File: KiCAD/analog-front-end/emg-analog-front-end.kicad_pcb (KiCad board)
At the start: 2 copper layers, 45 x 20 mm, 42 parts, among them J1 Conn_01x03, J2 Conn_01x03, J4 Conn_01x03_Female, J5 Conn_01x03_Female, J6 Conn_01x03_Female, J7 Conn_01x03_Female, U1 AD620, U2 LMC6482, U3 LMC6482, U4 LMC6482

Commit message: more progress on layout
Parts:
- added J3: Conn_01x03, Connector_PinHeader_1.27mm:PinHeader_1x03_P1.27mm_Vertical, F.Cu at (28.0, 18.5)
- moved C13 23.6 mm to (25.5, 15.9), turned to 90 degrees
- moved C16 19.7 mm to (35.8, 5.59), turned to 90 degrees
- moved J2 17.5 mm to (28.0, 1.50), turned to 90 degrees
- moved C12 14.5 mm to (35.1, 11.6), turned to 180 degrees
- moved C17 13.8 mm to (26.7, 9.40), turned to 90 degrees
- moved TP1 8.13 mm to (16.1, 3.17)
- moved R11 7.66 mm to (33.1, 2.29)
- moved R10 6.65 mm to (33.1, 1.14), turned to 0 degrees
- moved C8 6.52 mm to (10.5, 11.7), turned to -90 degrees
- moved R8 5.90 mm to (34.8, 1.65), turned to -90 degrees
- moved C7 5.35 mm to (11.7, 11.7), turned to -90 degrees
- moved C6 4.47 mm to (12.8, 11.7), turned to -90 degrees
- moved C5 4.07 mm to (14.0, 11.7), turned to -90 degrees
- moved H2 3.05 mm to (39.0, 17.0)
- moved H3 3.04 mm to (39.0, 3.00)
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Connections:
- net /AOUT_CH0 renamed AOUT_CH0
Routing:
- net AOUT_CH0: track 0.00 -> 24.2 mm
- net /AMP_IN-_CH0: track 0.00 -> 17.7 mm, vias 0 -> 2
- net VDD: track 0.00 -> 17.5 mm, vias 0 -> 2
- net /AMP_OUT_CH0: track 0.00 -> 17.0 mm, vias 0 -> 2
- net SK11: track 0.00 -> 11.6 mm
- net -5V: track 0.00 -> 7.82 mm
- net Net-(C10-Pad2): track 0.00 -> 7.79 mm, vias 0 -> 2
- net /AMP_IN+_CH0: track 0.00 -> 7.27 mm
- net SK01: track 0.00 -> 6.88 mm
- net Net-(C11-Pad1): track 0.00 -> 4.17 mm
- net /NOTCH_IN_CH0: track 0.00 -> 4.15 mm
- net SK00: track 0.00 -> 4.15 mm
- net /IA_OUT_CH0: track 0.00 -> 3.43 mm
- net /HPF_OUT_CH0: track 0.00 -> 3.43 mm
- net NOTCH_OUT_CH0: track 0.00 -> 3.42 mm
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- added copper zone on F.Cu, net GND
- added copper zone on B.Cu, net VDD
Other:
- board size 45 x 20 mm -> 42 x 20 mm
- board text added: "E+"
- board text added: "E-"
- board text added: "REF"

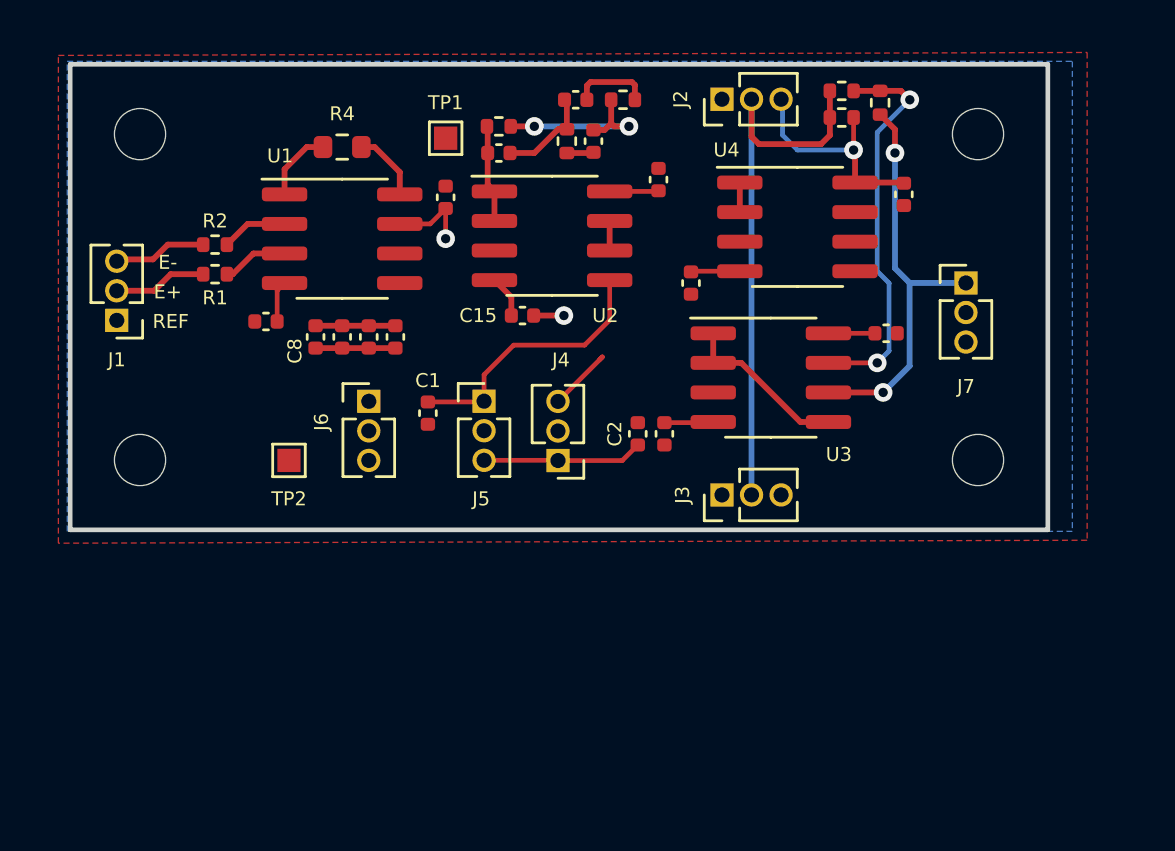
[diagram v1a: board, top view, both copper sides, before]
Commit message: AFE sub-circuit layout done
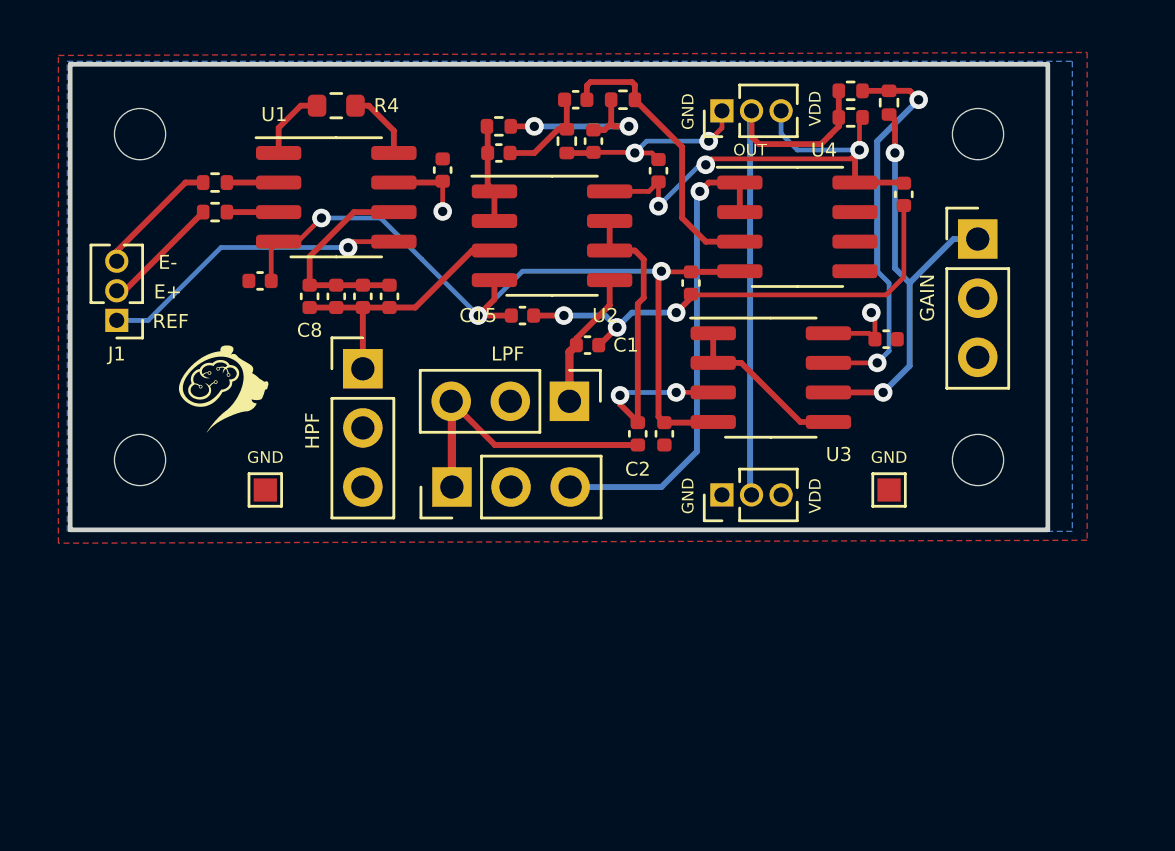
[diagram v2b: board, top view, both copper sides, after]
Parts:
- added G***: LOGO, LOGO, F.Cu at (6.60, 14.0)
- J4, J5, J6, J7: footprint Connector_PinHeader_1.27mm:PinHeader_1x03_P1.27mm_Vertical -> Connector_PinHeader_2.54mm:PinHeader_1x03_P2.54mm_Vertical
- moved TP1 24.3 mm to (35.2, 18.3)
- moved C1 7.45 mm to (22.2, 12.1), turned to 180 degrees
- moved J4 4.70 mm to (16.4, 18.2), turned to 90 degrees
- moved J5 3.67 mm to (21.4, 14.5), turned to -90 degrees
- moved R1 2.67 mm to (6.22, 6.35)
- moved R2 2.67 mm to (6.22, 5.08)
- moved J7 1.95 mm to (39.0, 7.51)
- moved U1 1.80 mm to (11.4, 5.71)
- moved R4 1.80 mm to (11.4, 1.78)
- moved C5 1.76 mm to (13.7, 9.97)
- moved C3 1.76 mm to (8.16, 9.31)
- moved C6 1.76 mm to (12.6, 9.97)
- moved C7 1.76 mm to (11.4, 9.97)
- moved C8 1.76 mm to (10.3, 9.97)
- moved TP2 1.63 mm to (8.38, 18.3)
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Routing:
- net GND: track 2.59 -> 43.8 mm, vias 1 -> 6
- net -5V: track 7.82 -> 36.6 mm, vias 0 -> 3
- net SK00: track 4.15 -> 20.4 mm, vias 0 -> 1
- net /LPF_IN-_CH0: track 1.27 -> 15.5 mm, vias 0 -> 2
- net VDD: track 17.5 -> 29.4 mm, vias 2 -> 5
- net NOTCH_OUT_CH0: track 3.42 -> 12.2 mm
- net /HPF_OUT_CH0: track 3.43 -> 11.6 mm
- net SK11: track 11.6 -> 5.92 mm
- net /IA_OUT_CH0: track 3.43 -> 9.04 mm
- net SK01: track 6.88 -> 12.5 mm
- net E2_CH0: track 4.01 -> 5.36 mm
- net /AMP_IN-_CH0: track 17.7 -> 18.8 mm
- net E1_CH0: track 4.01 -> 5.11 mm
- net AOUT_CH0: track 24.2 -> 23.4 mm
- net /IA_IN-_CH0: track 2.84 -> 2.22 mm
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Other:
- board text added: "GAIN"
- board text added: "GND"
- board text added: "HPF"
- board text added: "LPF"
- board text added: "OUT"
- board text added: "VDD"

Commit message: added VSS input to the AFE board
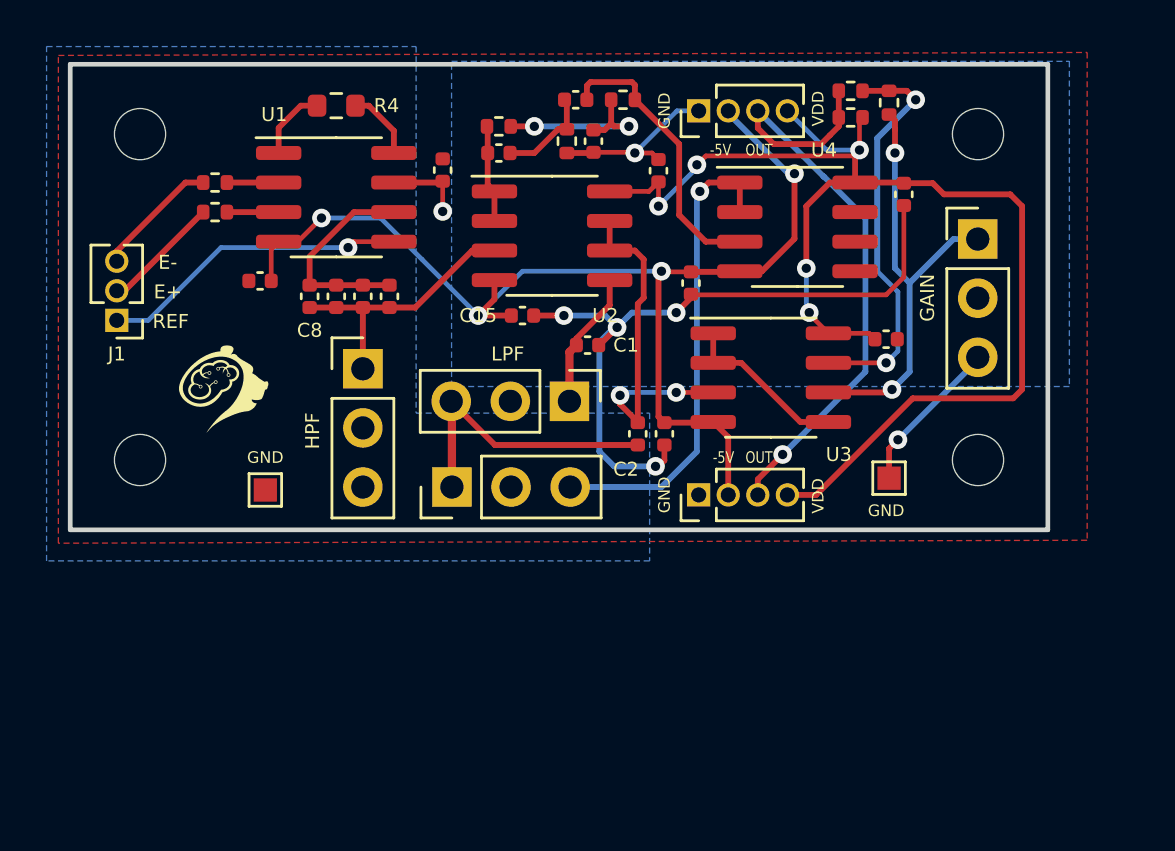
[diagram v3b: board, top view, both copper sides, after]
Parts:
- J2, J3: value Conn_01x03 -> Conn_01x04_Female; footprint Connector_PinHeader_1.27mm:PinHeader_1x03_P1.27mm_Vertical -> Connector_PinHeader_1.27mm:PinHeader_1x04_P1.27mm_Vertical
- moved J2 1.00 mm to (27.0, 2.00)
- moved J3 1.00 mm to (27.0, 18.5)
- moved TP1 0.51 mm to (35.2, 17.8)
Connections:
- J2 pad 2: AOUT_CH0 -> -5V
- J2 pad 3: VDD -> AOUT_CH0
- J3 pad 2: AOUT_CH0 -> -5V
- J3 pad 3: VDD -> AOUT_CH0
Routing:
- net VDD: track 29.4 -> 61.1 mm, vias 5 -> 6
- net GND: track 43.8 -> 58.7 mm, vias 6 -> 7
- net -5V: track 36.6 -> 49.7 mm, vias 3 -> 4
- net AOUT_CH0: track 23.4 -> 26.6 mm, vias 0 -> 1
- added copper zone on B.Cu, net -5V
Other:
- board text added: "-5V"
